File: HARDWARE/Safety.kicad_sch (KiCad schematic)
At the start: 5 parts, among them K1 FINDER-30.22, Q1 BSS138

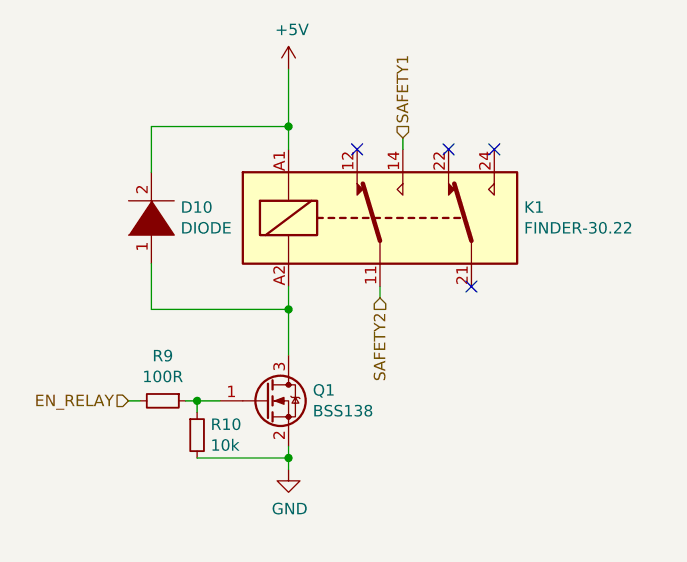
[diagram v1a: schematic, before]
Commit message: Align components on the PCB
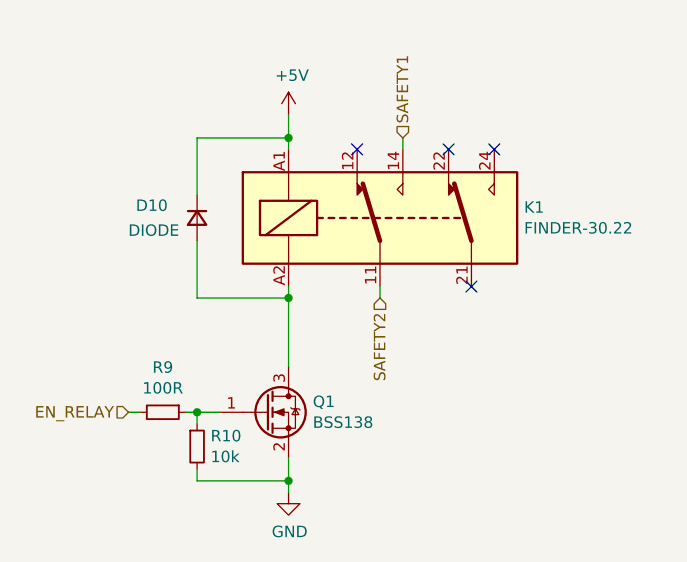
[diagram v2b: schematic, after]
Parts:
- D10: symbol pspice:DIODE -> Device:D_Small
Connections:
- net +5V: now also D10.1 (K); no longer D10.2 (A)
- net at K1.A2, Q1.3 (D): now also D10.2 (A); no longer D10.1 (K)
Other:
- company: (none) -> PUT Motorsport
- moved on the sheet: Q1, R10, R9

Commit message: Route PCB tracks
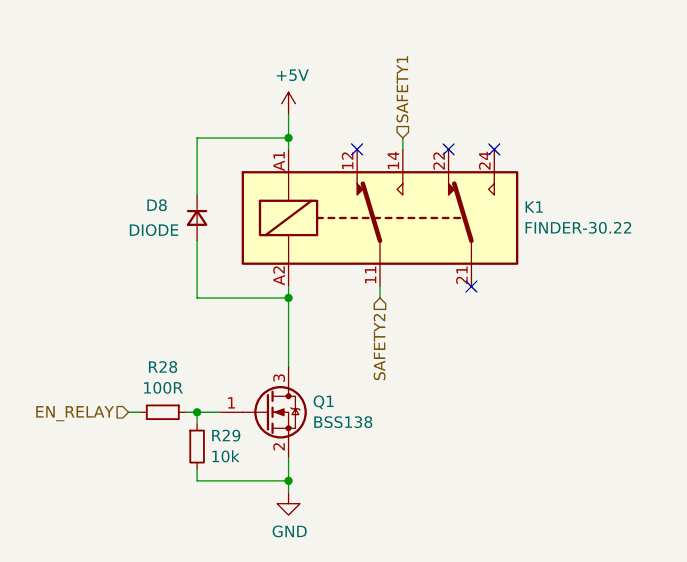
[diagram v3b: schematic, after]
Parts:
- renumbered D10 to D8, R9 to R28, R10 to R29
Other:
- company: PUT Motorsport -> S. Sambor
- title: (none) -> Safety Relay
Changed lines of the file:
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@@
   (paper "A4")
   (title_block
-    (company "PUT Motorsport")
-    (comment 1 "Patryk Gawron")
+    (title "Safety Relay")
+    (date "2023-04-22")
+    (rev "2.0")
+    (company "S. Sambor")
+    (comment 1 "J. Jurczak")
+    (comment 2 "P. Gawron")
+    (comment 3 "I. Kajdan")
   )
   (junction (at 143.51 82.55) (diameter 0) (color 0 0 0 0)
@@
   (symbol (lib_id "Device:D_Small") (at 133.35 91.44 270) (unit 1)
     (in_bom yes) (on_board yes) (dnp no)
-    (property "Reference" "D10" (at 130.0988 90.0684 90)
+    (property "Reference" "D8" (at 130.0988 90.0684 90)
       (effects (font (size 1.27 1.27)) (justify right))
     )
@@
       (project "APPS"
         (path "/fc4ad874-c922-4070-89f9-7262080469d8/00000000-0000-0000-0000-00005f99e99e"
-          (reference "D10") (unit 1)
+          (reference "D8") (unit 1)
         )
       )
@@
   (symbol (lib_id "Device:R_Small") (at 129.54 113.03 270) (unit 1)
     (in_bom yes) (on_board yes) (dnp no)
-    (property "Reference" "R9" (at 129.54 108.0516 90)
+    (property "Reference" "R28" (at 129.54 108.0516 90)
       (effects (font (size 1.27 1.27)))
     )
@@
       (project "APPS"
         (path "/fc4ad874-c922-4070-89f9-7262080469d8/00000000-0000-0000-0000-00005f99e99e"
-          (reference "R9") (unit 1)
+          (reference "R28") (unit 1)
         )
       )
@@
   (symbol (lib_id "Device:R_Small") (at 133.35 116.84 0) (unit 1)
     (in_bom yes) (on_board yes) (dnp no)
-    (property "Reference" "R10" (at 134.8486 115.6716 0)
+    (property "Reference" "R29" (at 134.8486 115.6716 0)
       (effects (font (size 1.27 1.27)) (justify left))
     )
@@
       (project "APPS"
         (path "/fc4ad874-c922-4070-89f9-7262080469d8/00000000-0000-0000-0000-00005f99e99e"
-          (reference "R10") (unit 1)
+          (reference "R29") (unit 1)
         )
       )
@@
   (symbol (lib_id "power:+5V") (at 143.51 80.01 0) (unit 1)
     (in_bom yes) (on_board yes) (dnp no)
-    (property "Reference" "#PWR023" (at 143.51 83.82 0)
+    (property "Reference" "#PWR048" (at 143.51 83.82 0)
       (effects (font (size 1.27 1.27)) hide)
     )
@@
       (project "APPS"
         (path "/fc4ad874-c922-4070-89f9-7262080469d8/00000000-0000-0000-0000-00005f99e99e"
-          (reference "#PWR023") (unit 1)
+          (reference "#PWR048") (unit 1)
         )
       )
@@
   (symbol (lib_id "power:GND") (at 143.51 121.92 0) (unit 1)
     (in_bom yes) (on_board yes) (dnp no)
-    (property "Reference" "#PWR024" (at 143.51 128.27 0)
+    (property "Reference" "#PWR049" (at 143.51 128.27 0)
       (effects (font (size 1.27 1.27)) hide)
     )
@@
       (project "APPS"
         (path "/fc4ad874-c922-4070-89f9-7262080469d8/00000000-0000-0000-0000-00005f99e99e"
-          (reference "#PWR024") (unit 1)
-        )
-      )
+          (reference "#PWR049") (unit 1)
+        )
+      )
